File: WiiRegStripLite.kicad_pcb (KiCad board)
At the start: 2 copper layers, 55.5 x 55 mm, 89 parts, among them J1 Conn_01x04_Socket, J2 Conn_01x04_Socket, U10 TLV62585DRL, U5 BQ25895RTW, U6 ATtiny1616-M, U7 TLV62585DRL, U8 TLV62585DRL, U9 TLV62585DRL

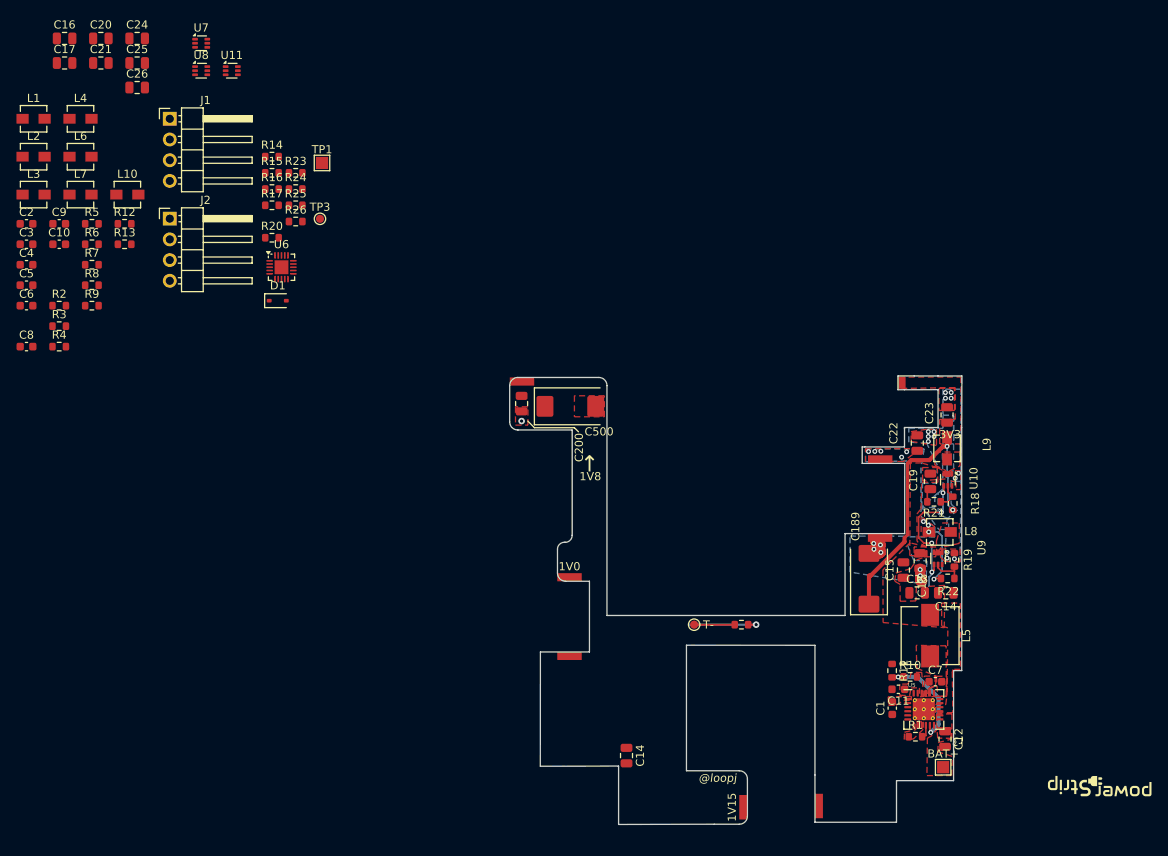
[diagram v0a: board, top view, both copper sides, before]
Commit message: More Reg Work, MCU placement
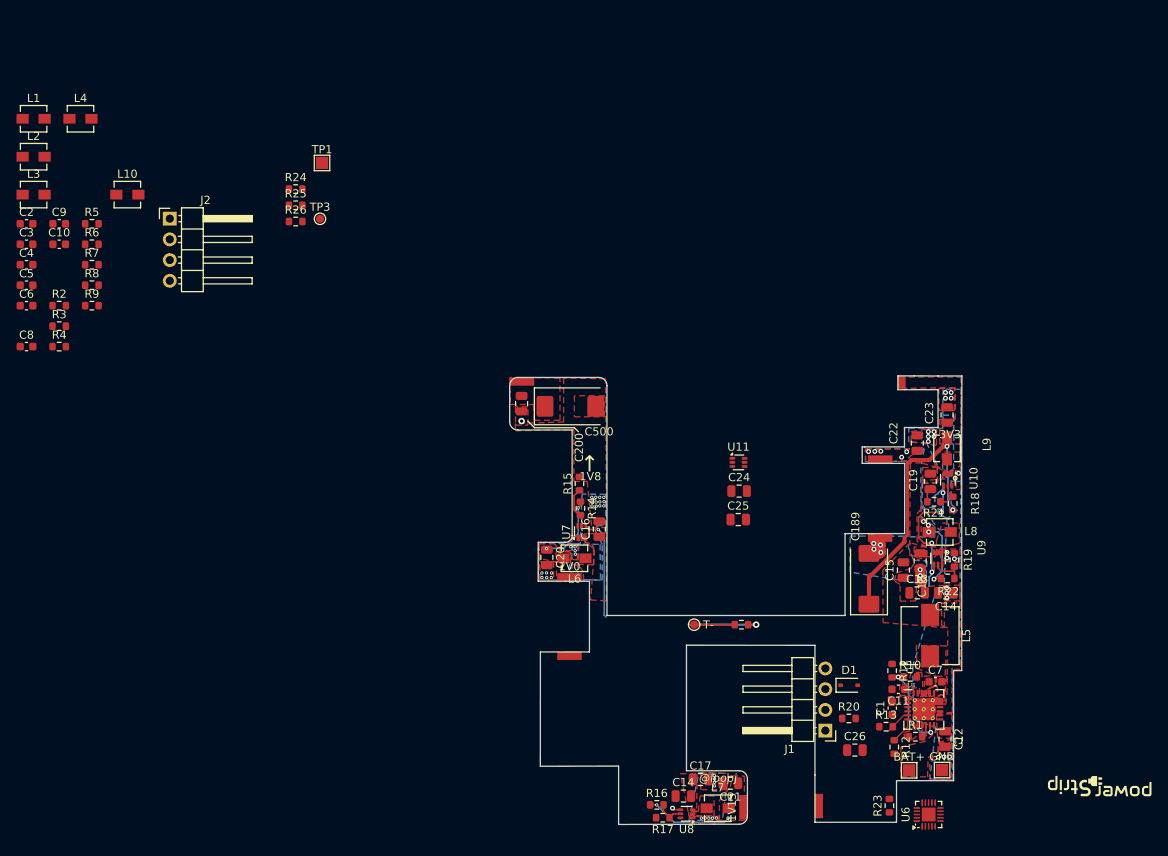
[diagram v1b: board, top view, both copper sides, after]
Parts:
- added GND: BAT+, TestPoint:TestPoint_Pad_1.5x1.5mm, F.Cu at (186.5, 151.8)
- moved C26 119.8 mm to (175.8, 149.3)
- moved C17 117.5 mm to (156.9, 153.0)
- moved C21 117.3 mm to (160.5, 153.4), turned to 180 degrees
- moved R12 114.1 mm to (180.6, 149.0), turned to -90 degrees
- moved R13 110.5 mm to (179.6, 146.5)
- moved J1 110.0 mm to (172.2, 147.0), turned to 180 degrees
- moved U8 108.8 mm to (155.2, 157.2), turned to 180 degrees
- moved L7 108.5 mm to (159.0, 156.5)
- moved R23 106.4 mm to (180.0, 156.2), turned to 90 degrees
- moved U6 103.9 mm to (184.8, 157.2), turned to 90 degrees
- moved C25 92.6 mm to (161.5, 121.1)
- moved C24 92.4 mm to (161.6, 117.6)
- moved R20 92.1 mm to (175.1, 145.5)
- moved R17 89.1 mm to (152.2, 157.6), turned to 180 degrees
- moved R16 89.1 mm to (151.5, 156.1)
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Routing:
- net EN: track 17.3 -> 31.3 mm, vias 4 -> 6
- net 1V08: track 0.00 -> 10.8 mm, vias 0 -> 2
- net 1V: track 0.00 -> 8.74 mm, vias 0 -> 2
- net GND: track 9.73 -> 18.3 mm, vias 22 -> 59
- net Net-(U7-FB): track 0.00 -> 5.07 mm
- net Net-(U8-FB): track 0.00 -> 3.41 mm
- net SDA: track 0.00 -> 3.24 mm
- net SCL: track 0.00 -> 3.23 mm
- net Net-(U5-TS): track 13.0 -> 11.5 mm
- added copper zone on F.Cu, net /L1v
- added copper zone on F.Cu, net /L1v08
- added copper zone on F.Cu, net 1V
- added copper zone on F.Cu, net 1V08
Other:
- outline, holes or cut-outs redrawn

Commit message: More work
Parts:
- removed C10, C3, C5, C6: 22uF, Capacitor_SMD:C_0603_1608Metric
- removed C2, C4, C8, C9: 4.7uF, Capacitor_SMD:C_0603_1608Metric
- removed L1: 1uH, Inductor_SMD:L_Vishay_IHLP-1212
- removed L2, L3, L4: 2.2uH, Inductor_SMD:L_Vishay_IHLP-1212
- removed R2: 124k, Resistor_SMD:R_0603_1608Metric
- removed R3, R5, R7, R9: 100k, Resistor_SMD:R_0603_1608Metric
- removed R4: 414k, Resistor_SMD:R_0603_1608Metric
- removed R6, R8: 66.5k, Resistor_SMD:R_0603_1608Metric
- removed TP6: T-, TestPoint:TestPoint_Pad_D1.0mm
- added J3: Fan, Connector_PinHeader_2.54mm:PinHeader_1x02_P2.54mm_Vertical, F.Cu at (176.9, 156.8)
- added R27: 10k, Resistor_SMD:R_0603_1608Metric, F.Cu at (159.5, 135.0)
- added TP60: TestPoint, TestPoint:TestPoint_Pad_D1.0mm, F.Cu at (180.1, 154.2)
- J1, J2: footprint Connector_PinHeader_2.54mm:PinHeader_1x04_P2.54mm_Horizontal -> Connector_PinHeader_2.54mm:PinHeader_1x04_P2.54mm_Vertical
- TH1: value Thermistor_NTC -> 10k
- moved TP1 84.2 mm to (151.9, 150.7)
- moved L10 82.4 mm to (141.0, 143.2), turned to 180 degrees
- moved TP3 82.2 mm to (148.3, 157.1)
- moved J2 80.7 mm to (139.0, 149.6), turned to 90 degrees
- moved R24 78.0 mm to (149.2, 146.2), turned to 90 degrees
- moved R25 75.5 mm to (147.7, 146.2), turned to -90 degrees
- moved R26 70.5 mm to (146.9, 142.7), turned to 90 degrees
- moved U11 34.2 mm to (144.8, 143.8), turned to 180 degrees
- moved C24 32.8 mm to (145.2, 146.0)
- moved C25 31.9 mm to (141.7, 146.0), turned to 180 degrees
- moved D1 12.2 mm to (174.0, 153.6), turned to -90 degrees
- moved R20 11.3 mm to (174.3, 156.8), turned to -90 degrees
- moved U6 10.2 mm to (177.1, 150.7)
- moved C26 4.68 mm to (177.2, 153.8), turned to 180 degrees
- moved R23 4.17 mm to (180.1, 152.0)
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- renumbered BAT+ to B+
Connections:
- TH1 pad 1: (no net) -> PA1
- TH1 pad 2: (no net) -> GND
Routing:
- net GND: track 18.3 -> 36.0 mm, vias 59 -> 61
- net VIN: track 0.00 -> 17.6 mm, vias 0 -> 3
- net Net-(D1-A): track 0.00 -> 16.2 mm
- net (no net): track 14.2 -> 0.00 mm, vias 1 -> 0
- net Net-(D1-K): track 0.00 -> 8.71 mm
- net UPDI: track 0.00 -> 7.68 mm
- net 5V: track 0.00 -> 6.15 mm
- net PA4: track 0.00 -> 5.72 mm, vias 0 -> 1
- net SCL: track 3.23 -> 7.81 mm, vias 0 -> 1
- net SDA: track 3.24 -> 7.45 mm, vias 0 -> 1
- net Net-(U11-FB): track 0.00 -> 4.12 mm
- net PA2: track 0.00 -> 2.32 mm, vias 0 -> 1
- net PA7: track 0.00 -> 2.27 mm
- net Net-(U11-EN): track 0.00 -> 1.52 mm
- net NeoPixelDIN: track 0.00 -> 1.42 mm
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- added copper zone on F.Cu, net /L5v
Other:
- outline, holes or cut-outs redrawn
- board text removed: "JLCJLCJLCJLC"

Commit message: Final Design
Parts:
- J2: footprint Connector_PinHeader_2.54mm:PinHeader_1x04_P2.54mm_Vertical -> Connector_PinHeader_2.54mm:PinHeader_1x05_P2.54mm_Vertical
- moved TP1 25.2 mm to (176.5, 145.1)
- moved R27 5.89 mm to (154.3, 137.7), turned to -90 degrees
- moved TH1 5.15 mm to (158.2, 135.8)
- moved TP3 4.73 mm to (150.5, 152.9)
- moved C25 1.21 mm to (140.5, 145.9)
- moved R24 1.20 mm to (148.0, 146.1)
- moved C24 1.20 mm to (144.0, 145.9)
- moved L10 1.20 mm to (139.8, 143.1)
- moved R25 1.20 mm to (146.5, 146.1)
- moved R26 1.20 mm to (145.8, 142.6)
- moved U11 1.20 mm to (143.6, 143.7)
- moved C1 1.06 mm to (179.6, 143.4), turned to 0 degrees
- moved J2 0.51 mm to (138.6, 149.8)
- moved C189 0.43 mm to (177.2, 128.1)
- renumbered B+ to TP2
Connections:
- J2 pad 1: NeoPixelDO -> GND
- J2 pad 2: GND -> 5V
- J2 pad 3: 5V -> TX
- J2 pad 4: NeoPixelDIN -> RX
- U6 pad 1: PA2 -> EN
- U6 pad 6: PA5 -> BTN
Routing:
- net EN: track 31.3 -> 146.9 mm, vias 6 -> 13
- net BTN: track 0.00 -> 79.0 mm, vias 0 -> 2
- net TX: track 0.00 -> 63.6 mm, vias 0 -> 2
- net RX: track 0.00 -> 61.9 mm, vias 0 -> 2
- net PA1: track 0.79 -> 39.0 mm, vias 1 -> 2
- net GND: track 36.0 -> 65.3 mm, vias 61 -> 105
- net VIN: track 17.6 -> 21.9 mm, vias 3 -> 4
- net Net-(D1-K): track 8.71 -> 11.3 mm, vias 0 -> 2
- net PA2: track 2.32 -> 0.00 mm, vias 1 -> 0
- net 3V: track 35.8 -> 37.0 mm
- net 5V: track 6.15 -> 7.10 mm
- net PA4: track 5.72 -> 5.77 mm, vias 1 -> 2
- added copper zone on F.Cu, net 5V
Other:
- outline, holes or cut-outs redrawn
- board text added: "1V35"
- board text added: "@dekunut"
- board text added: "HAVOC"
- board text removed: "1V8"
- board text removed: "r3"

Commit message: Gerber gen and new ibom
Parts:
- U11: value ~ -> TPS61023DRLR
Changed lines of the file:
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@@
 			(plot_on_all_layers_selection 0x0000000_00000000)
 			(disableapertmacros no)
-			(usegerberextensions no)
+			(usegerberextensions yes)
 			(usegerberattributes yes)
 			(usegerberadvancedattributes yes)
-			(creategerberjobfile yes)
+			(creategerberjobfile no)
 			(dashed_line_dash_ratio 12.000000)
 			(dashed_line_gap_ratio 3.000000)
@@
 			(psa4output no)
 			(plotreference yes)
-			(plotvalue yes)
+			(plotvalue no)
 			(plotfptext yes)
 			(plotinvisibletext no)
 			(sketchpadsonfab no)
-			(subtractmaskfromsilk no)
+			(subtractmaskfromsilk yes)
 			(outputformat 1)
 			(mirror no)
-			(drillshape 1)
+			(drillshape 0)
 			(scaleselection 1)
 			(outputdirectory "")
@@
 			)
 		)
-		(property "Value" "~"
+		(property "Value" "TPS61023DRLR"
 			(at 0 1.75 180)
 			(layer "F.Fab")

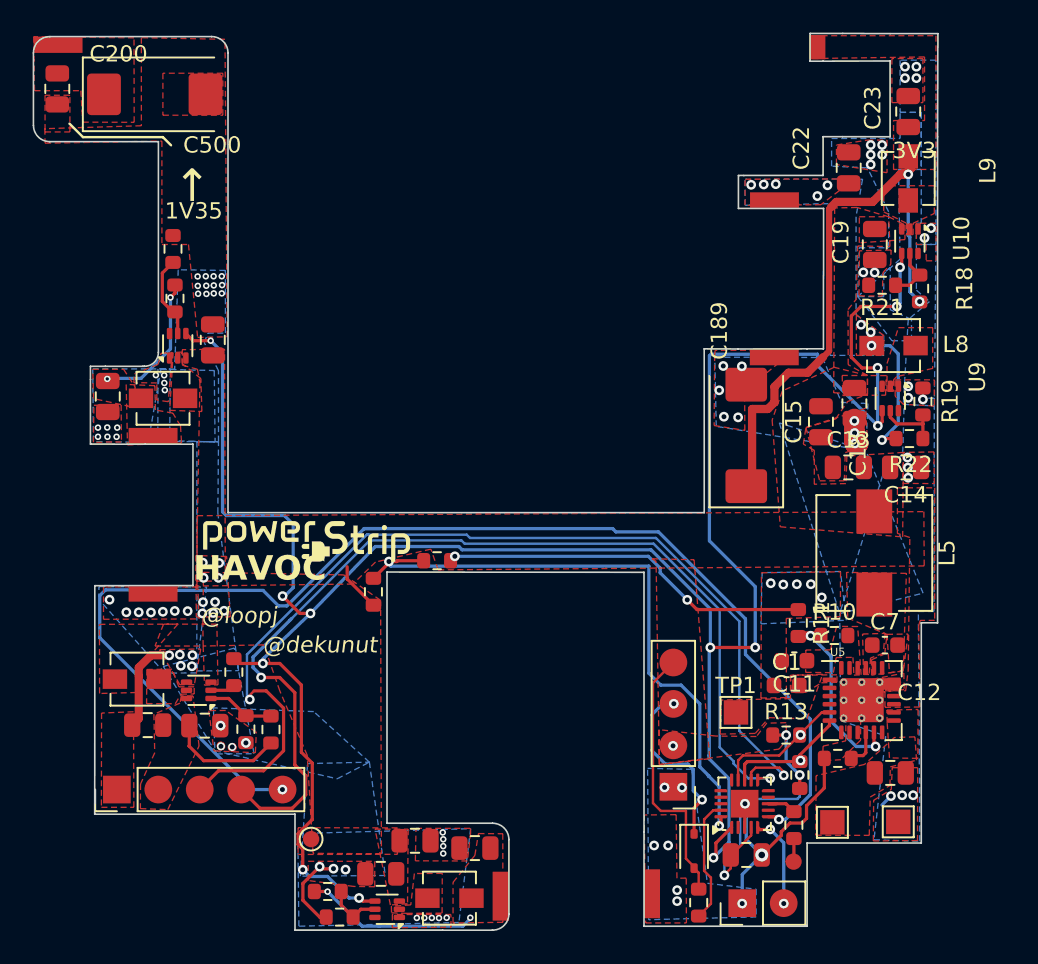
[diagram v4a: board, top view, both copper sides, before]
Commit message: More edits
Rounded edges, moved traces, added EN pull down resistor
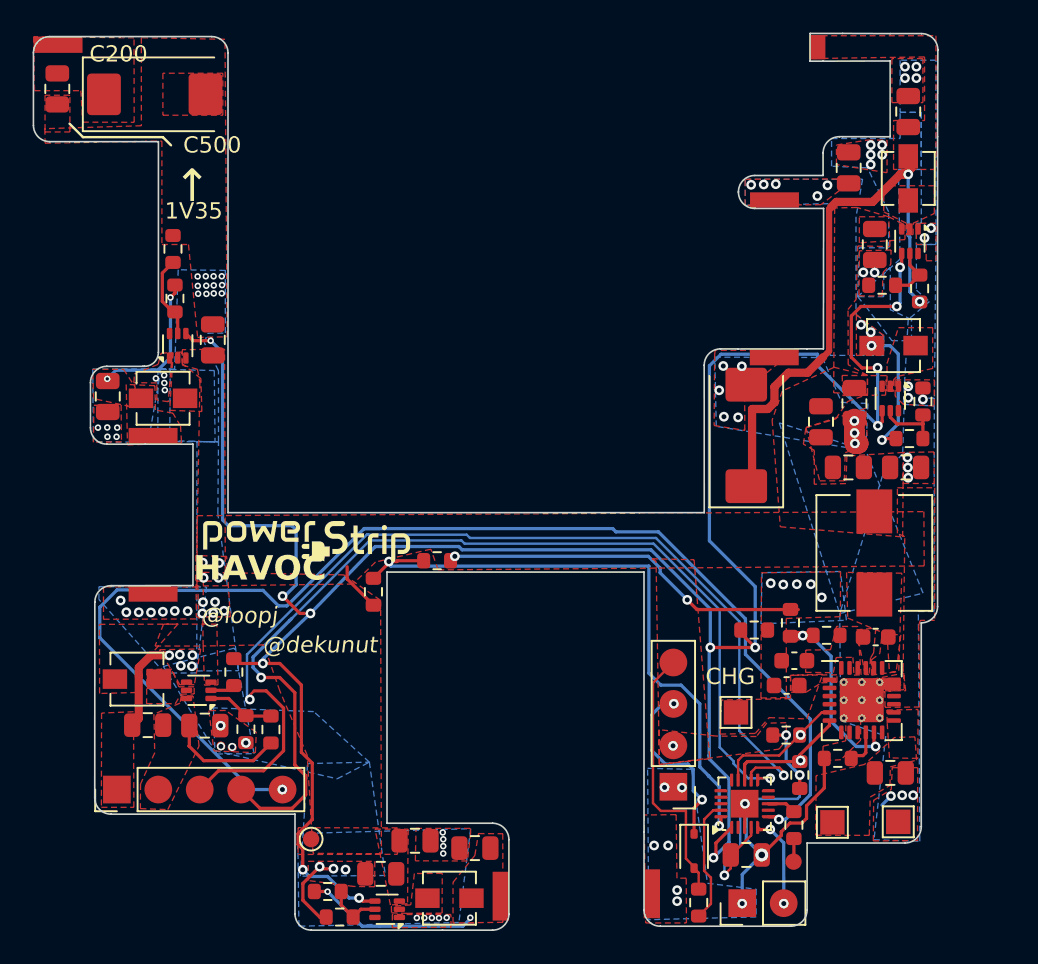
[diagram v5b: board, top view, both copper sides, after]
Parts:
- added R28: 10k, Resistor_SMD:R_0603_1608Metric, F.Cu at (177.7, 140.0)
- moved C7 0.75 mm to (185.1, 140.5)
- moved R11 0.48 mm to (179.9, 139.6)
- moved R10 0.48 mm to (182.1, 140.4)
- renumbered TP1 to CHG
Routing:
- net EN: track 146.9 -> 148.3 mm
- net GND: track 65.3 -> 65.2 mm, vias 105 -> 104
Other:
- outline, holes or cut-outs redrawn
